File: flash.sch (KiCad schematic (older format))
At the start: 1 part, among them U1 SST25VF032B

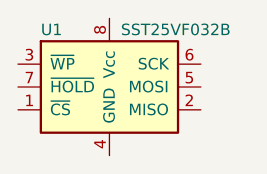
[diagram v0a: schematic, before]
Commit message: fpga chip placed in the schematic "fpga" sheet and on the PCB.
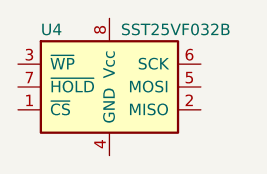
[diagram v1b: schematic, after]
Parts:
- renumbered U1 to U4
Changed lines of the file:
@@
 LIBS:contrib
 LIBS:valves
+LIBS:lfxp2-xe-xtn144x
 LIBS:ulx2s-cache
 EELAYER 25 0
@@
 $Descr A4 11693 8268
 encoding utf-8
-Sheet 6 6
+Sheet 6 7
 Title ""
 Date ""
@@
 $EndDescr
 $Comp
-L MB85RS16 U1
+L MB85RS16 U4
 U 1 1 5A12E0C4
 P 2850 2600
-F 0 "U1" H 2550 2850 50  0000 L CNN
+F 0 "U4" H 2550 2850 50  0000 L CNN
 F 1 "SST25VF032B" H 2900 2850 50  0000 L CNN
 F 2 "SOA008-150mil:SOA008-150mil" H 2500 2550 50  0001 C CNN
